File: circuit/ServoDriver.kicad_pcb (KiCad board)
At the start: 2 copper layers, 95 x 54.5 mm, 47 parts, among them IC1 TLP521, IC2 TLP521, IC3 TLP521, IC4 TLP521, IC5 TLP521, IC6 TLP521, J1 RJ45_8pin, J2 RJ45_8pin, J3 servo0, J4 servo1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

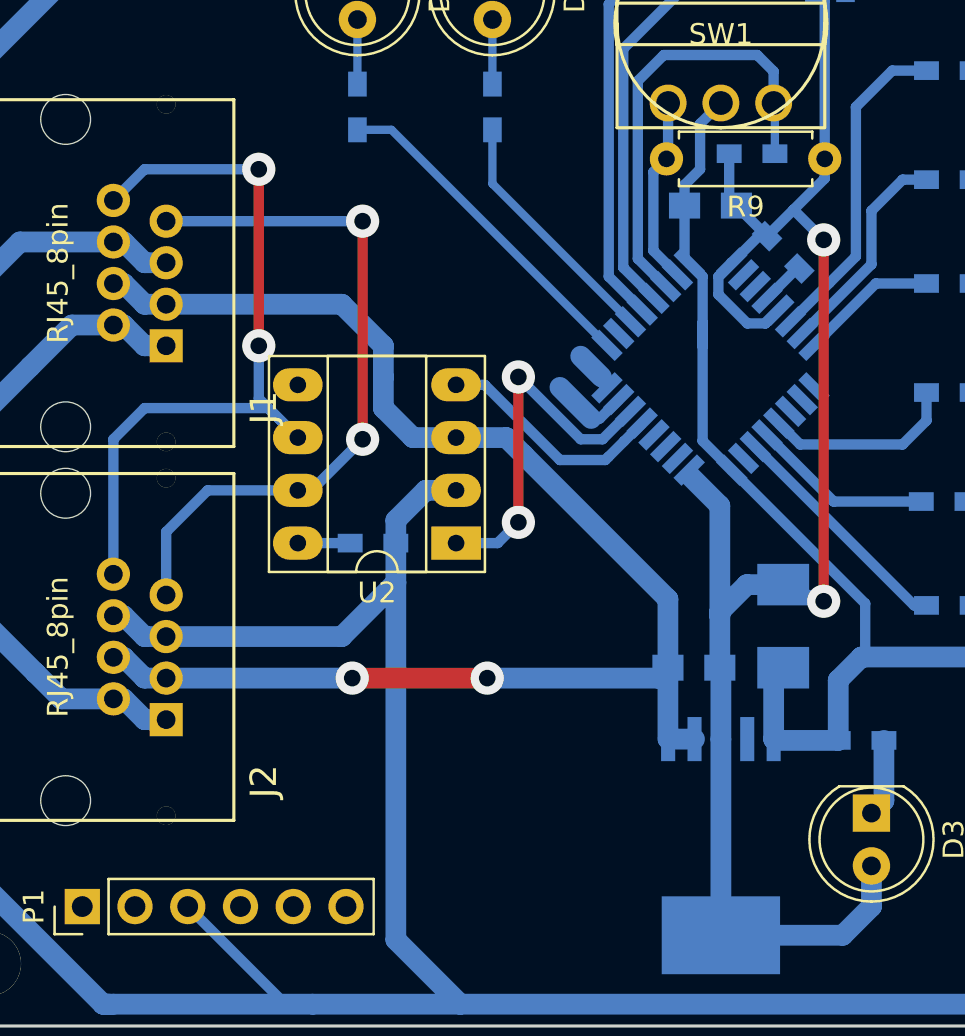
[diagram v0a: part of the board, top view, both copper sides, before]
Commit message: SWDのところにパッドを追加
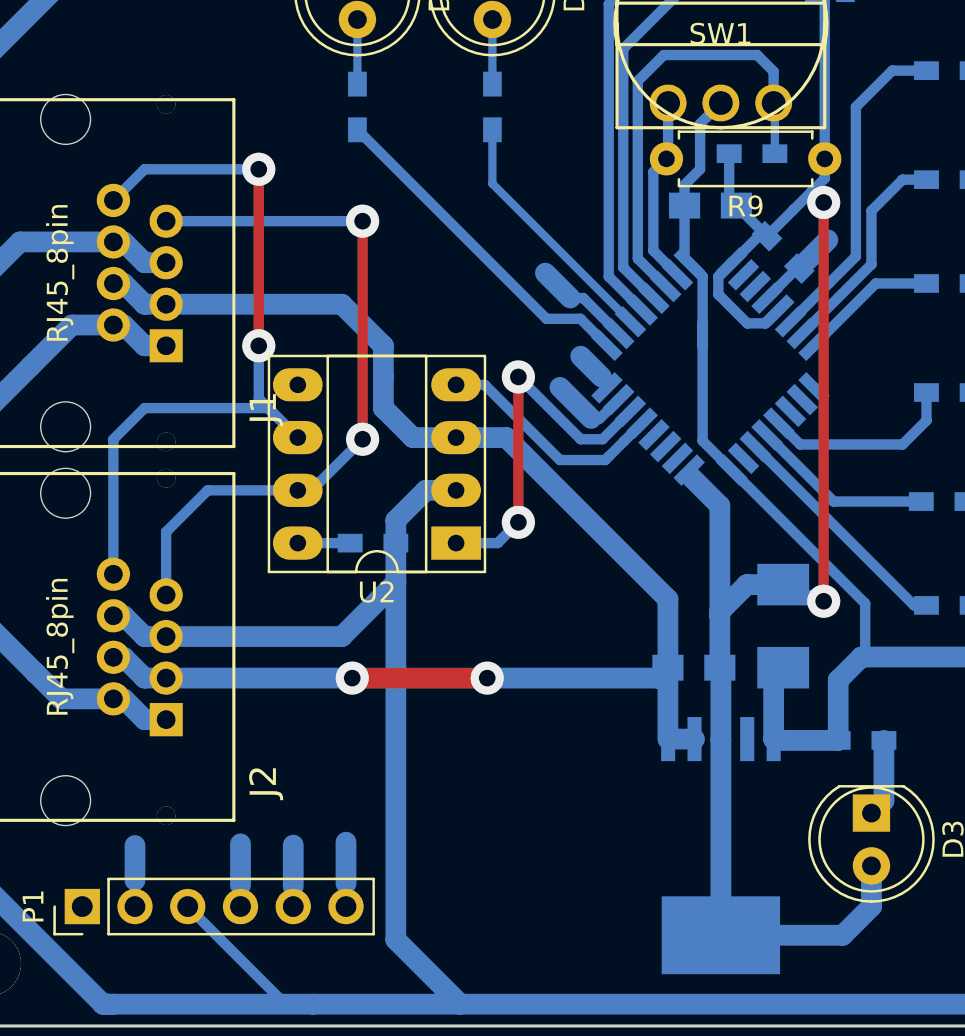
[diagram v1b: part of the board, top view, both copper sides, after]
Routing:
- net /SWO: track 0.00 -> 7.84 mm
- net /NRST: track 2.15 -> 7.06 mm
- net /SWDIO: track 3.83 -> 6.85 mm
- net /SWCLK: track 2.09 -> 5.03 mm
- net +3V3: track 85.5 -> 86.8 mm
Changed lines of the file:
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@@
     (thickness 1.6)
     (drawings 7)
-    (tracks 378)
+    (tracks 395)
     (zones 0)
     (modules 47)
@@
   )
   (setup
-    (last_trace_width 0.5)
+    (last_trace_width 1)
     (user_trace_width 0.4)
     (user_trace_width 1)
@@
   (segment (start 163.5 106) (end 163.5 97.75) (width 1.5) (layer B.Cu) (net 2))
   (segment (start 163.5 97.75) (end 163.5 91) (width 1.5) (layer B.Cu) (net 2))
-  (segment (start 130.747183 94.947183) (end 132.2 96.4) (width 0.5) (layer B.Cu) (net 3))
-  (segment (start 132.2 113.8) (end 130.25 113) (width 0.5) (layer B.Cu) (net 3) (status 800000))
+  (segment (start 132.2 94.6) (end 131.647183 94.047183) (width 0.5) (layer B.Cu) (net 3))
+  (segment (start 130.25 113) (end 132.2 113.8) (width 0.5) (layer B.Cu) (net 3))
   (via (at 132.2 113.8) (size 1.6) (drill 0.8) (layers F.Cu B.Cu) (net 3))
-  (segment (start 132.2 96.4) (end 132.2 113.8) (width 0.5) (layer F.Cu) (net 3))
-  (via (at 132.2 96.4) (size 1.6) (drill 0.8) (layers F.Cu B.Cu) (net 3))
+  (segment (start 132.2 94.6) (end 132.2 113.8) (width 0.5) (layer F.Cu) (net 3))
+  (via (at 132.2 94.6) (size 1.6) (drill 0.8) (layers F.Cu B.Cu) (net 3))
+  (segment (start 132.2 94.6) (end 131.647183 94.047183) (width 0.5) (layer B.Cu) (net 3))
   (segment (start 127.25052 120.4365) (end 127.25052 117.05052) (width 1) (layer B.Cu) (net 3))
   (segment (start 127.25052 117.05052) (end 127.2 117) (width 1) (layer B.Cu) (net 3))
@@
   (segment (start 131.75 84.35) (end 133.25 84.35) (width 0.5) (layer B.Cu) (net 3))
   (segment (start 129.472183 96.222183) (end 130.747183 94.947183) (width 0.5) (layer B.Cu) (net 3))
-  (segment (start 130.747183 94.947183) (end 132.25 93.444366) (width 0.5) (layer B.Cu) (net 3))
+  (segment (start 130.747183 94.947183) (end 131.6 94.094366) (width 0.5) (layer B.Cu) (net 3))
+  (segment (start 131.6 94.094366) (end 132.25 93.444366) (width 0.5) (layer B.Cu) (net 3))
   (segment (start 132.25 93.444366) (end 132.25 92.5) (width 0.5) (layer B.Cu) (net 3))
   (segment (start 132.25 92.5) (end 132.25 84.85) (width 0.5) (layer B.Cu) (net 3))
@@
   (segment (start 129.068019 96.222183) (end 129.472183 96.222183) (width 0.5) (layer B.Cu) (net 3))
   (segment (start 127.775305 97.514897) (end 127.75 97.489592) (width 0.5) (layer B.Cu) (net 3))
-  (segment (start 101.58 128.5) (end 106.28 133.2) (width 0.5) (layer B.Cu) (net 4) (status 400000))
+  (segment (start 101.58 128.5) (end 106.28 133.2) (width 0.5) (layer B.Cu) (net 4))
   (segment (start 106.28 133.2) (end 107.6 133.2) (width 0.5) (layer B.Cu) (net 4))
-  (segment (start 127.775305 107.485103) (end 134.2 113.909798) (width 0.5) (layer B.Cu) (net 4) (status 400000))
+  (segment (start 127.775305 107.485103) (end 134.2 113.909798) (width 0.5) (layer B.Cu) (net 4))
   (segment (start 134.2 113.909798) (end 134.2 116.484) (width 0.5) (layer B.Cu) (net 4))
-  (segment (start 98 96.5) (end 93.5 96.5) (width 1) (layer B.Cu) (net 4) (status 400000))
+  (segment (start 98 96.5) (end 93.5 96.5) (width 1) (layer B.Cu) (net 4))
   (segment (start 93.5 96.5) (end 90.5 99.5) (width 1) (layer B.Cu) (net 4))
-  (segment (start 111.6 111) (end 111.6 109.9) (width 0.5) (layer B.Cu) (net 4) (status 400000))
+  (segment (start 111.6 111) (end 111.6 109.9) (width 0.5) (layer B.Cu) (net 4))
   (segment (start 111.6 112.9) (end 111.6 130.1) (width 1) (layer B.Cu) (net 4))
   (segment (start 111.6 130.1) (end 114.7 133.2) (width 1) (layer B.Cu) (net 4))
@@
   (segment (start 158.5 118.25) (end 158.5 121) (width 1) (layer B.Cu) (net 20))
   (segment (start 156.734 116.484) (end 158.5 118.25) (width 1) (layer B.Cu) (net 20))
-  (segment (start 106.88 108.46) (end 107.54 108.46) (width 0.5) (layer B.Cu) (net 21) (status C00000))
-  (segment (start 107.54 108.46) (end 110 106) (width 0.5) (layer B.Cu) (net 21) (status 400000))
-  (segment (start 110 95.5) (end 100.54 95.5) (width 0.5) (layer B.Cu) (net 21) (status 800000))
+  (segment (start 106.88 108.46) (end 107.54 108.46) (width 0.5) (layer B.Cu) (net 21))
+  (segment (start 107.54 108.46) (end 110 106) (width 0.5) (layer B.Cu) (net 21))
+  (segment (start 110 95.5) (end 100.54 95.5) (width 0.5) (layer B.Cu) (net 21))
   (via (at 110 95.5) (size 1.6) (drill 0.8) (layers F.Cu B.Cu) (net 21))
   (segment (start 110 106) (end 110 95.5) (width 0.5) (layer F.Cu) (net 21))
@@
   (segment (start 98.5 100.5) (end 99.5 101.5) (width 1) (layer B.Cu) (net 22))
   (segment (start 99.5 101.5) (end 100.54 101.5) (width 1) (layer B.Cu) (net 22))
-  (segment (start 106.88 105.92) (end 105 104.04) (width 0.5) (layer B.Cu) (net 23) (status 400000))
-  (segment (start 99.5 93) (end 98 94.5) (width 0.5) (layer B.Cu) (net 23) (status 800000))
+  (segment (start 106.88 105.92) (end 105 104.04) (width 0.5) (layer B.Cu) (net 23))
+  (segment (start 99.5 93) (end 98 94.5) (width 0.5) (layer B.Cu) (net 23))
   (segment (start 105 93) (end 99.5 93) (width 0.5) (layer B.Cu) (net 23))
   (via (at 105 93) (size 1.6) (drill 0.8) (layers F.Cu B.Cu) (net 23))
@@
   (segment (start 99.5 104.5) (end 105.46 104.5) (width 0.5) (layer B.Cu) (net 23))
   (segment (start 98 106) (end 99.5 104.5) (width 0.5) (layer B.Cu) (net 23))
+  (segment (start 99.04 128.5) (end 99.04 127.24) (width 0.5) (layer B.Cu) (net 25) (status 400000))
+  (segment (start 99.04 127.24) (end 99.04 125.56) (width 1) (layer B.Cu) (net 25))
   (segment (start 121.764897 103.525305) (end 121.5 103.260408) (width 0.5) (layer B.Cu) (net 25))
   (segment (start 121.5 103) (end 120.5 102) (width 1) (layer B.Cu) (net 25))
   (segment (start 121.5 103.260408) (end 121.5 103) (width 0.5) (layer B.Cu) (net 25))
   (segment (start 121.764897 103.525305) (end 121.739592 103.5) (width 0.5) (layer B.Cu) (net 25))
+  (segment (start 104.12 128.5) (end 104.12 127.48) (width 0.5) (layer B.Cu) (net 26) (status 400000))
+  (segment (start 104.12 127.48) (end 104.12 125.48) (width 1) (layer B.Cu) (net 26))
   (segment (start 122.330583 104.09099) (end 121.421573 105) (width 0.5) (layer B.Cu) (net 26))
   (segment (start 121 105) (end 119.5 103.5) (width 1) (layer B.Cu) (net 26))
   (segment (start 121.421573 105) (end 121 105) (width 0.5) (layer B.Cu) (net 26))
+  (segment (start 106.66 128.5) (end 106.66 127.54) (width 0.5) (layer B.Cu) (net 27) (status 400000))
+  (segment (start 106.66 127.54) (end 106.66 125.54) (width 1) (layer B.Cu) (net 27))
+  (segment (start 131.027817 97.777817) (end 131.4 97.405634) (width 0.5) (layer B.Cu) (net 27) (status 400000))
+  (segment (start 131.4 97.4) (end 132.4 96.4) (width 1) (layer B.Cu) (net 27))
+  (segment (start 131.4 97.405634) (end 131.4 97.4) (width 0.5) (layer B.Cu) (net 27))
   (segment (start 129.472361 99.211953) (end 130.906497 97.777817) (width 0.5) (layer B.Cu) (net 27))
   (segment (start 130.906497 97.777817) (end 131.027817 97.777817) (width 0.5) (layer B.Cu) (net 27))
+  (segment (start 109.2 128.5) (end 109.2 127.4) (width 0.5) (layer B.Cu) (net 28) (status 400000))
+  (segment (start 109.2 127.4) (end 109.2 125.4) (width 1) (layer B.Cu) (net 28))
+  (segment (start 122.330583 100.90901) (end 120.621573 99.2) (width 0.5) (layer B.Cu) (net 28) (status 400000))
+  (segment (start 120 99.2) (end 118.8 98) (width 1) (layer B.Cu) (net 28))
+  (segment (start 120.621573 99.2) (end 120 99.2) (width 0.5) (layer B.Cu) (net 28))
   (segment (start 116.25 91.1) (end 116.25 93.697056) (width 0.4) (layer B.Cu) (net 29))
   (segment (start 116.25 93.697056) (end 122.896268 100.343324) (width 0.4) (layer B.Cu) (net 29))
-  (segment (start 121.764897 101.474695) (end 111.390202 91.1) (width 0.4) (layer B.Cu) (net 30))
-  (segment (start 111.390202 91.1) (end 109.75 91.1) (width 0.4) (layer B.Cu) (net 30))
+  (segment (start 121.764897 101.474695) (end 120.490202 100.2) (width 0.5) (layer B.Cu) (net 30) (status 400000))
+  (segment (start 118.85 100.2) (end 109.75 91.1) (width 0.5) (layer B.Cu) (net 30) (status 800000))
+  (segment (start 120.490202 100.2) (end 118.85 100.2) (width 0.5) (layer B.Cu) (net 30))
   (segment (start 106.88 111) (end 109.4 111) (width 0.5) (layer B.Cu) (net 31))
   (segment (start 124.71 82.19) (end 126.4 80.5) (width 0.5) (layer B.Cu) (net 32))

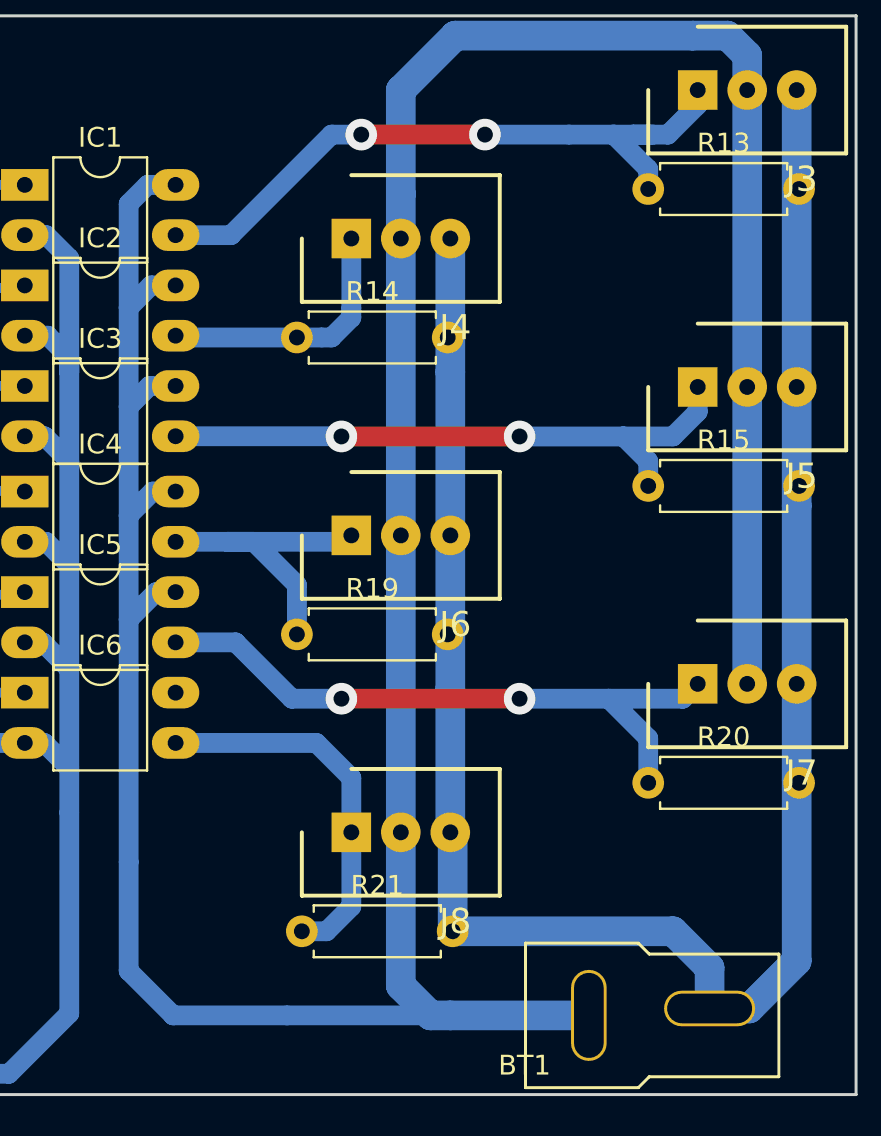
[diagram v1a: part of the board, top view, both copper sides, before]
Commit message: 基板加工用にデータを変更したやつを追加
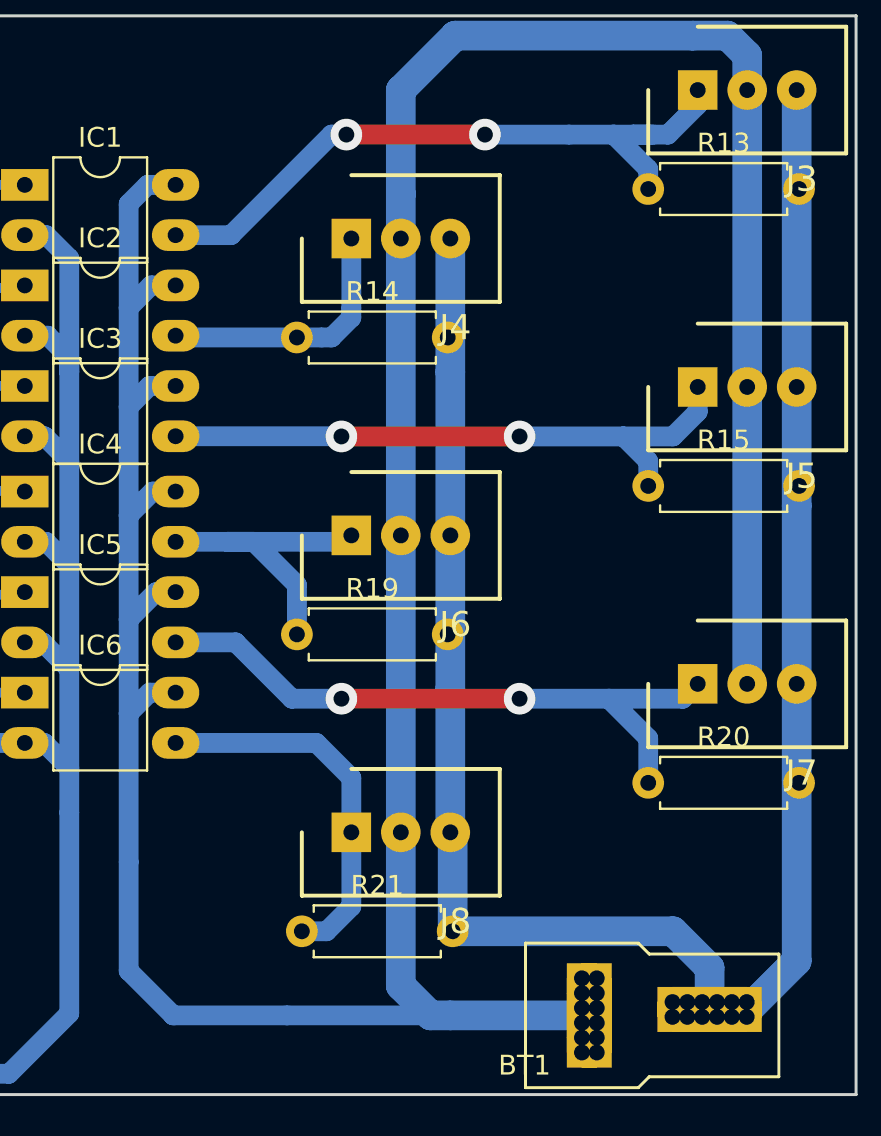
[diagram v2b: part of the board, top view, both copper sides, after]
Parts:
- BT1: footprint YASU:XT_M -> YASU:XT_Mdot
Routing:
- net +7.4V: track 176.3 -> 179.2 mm

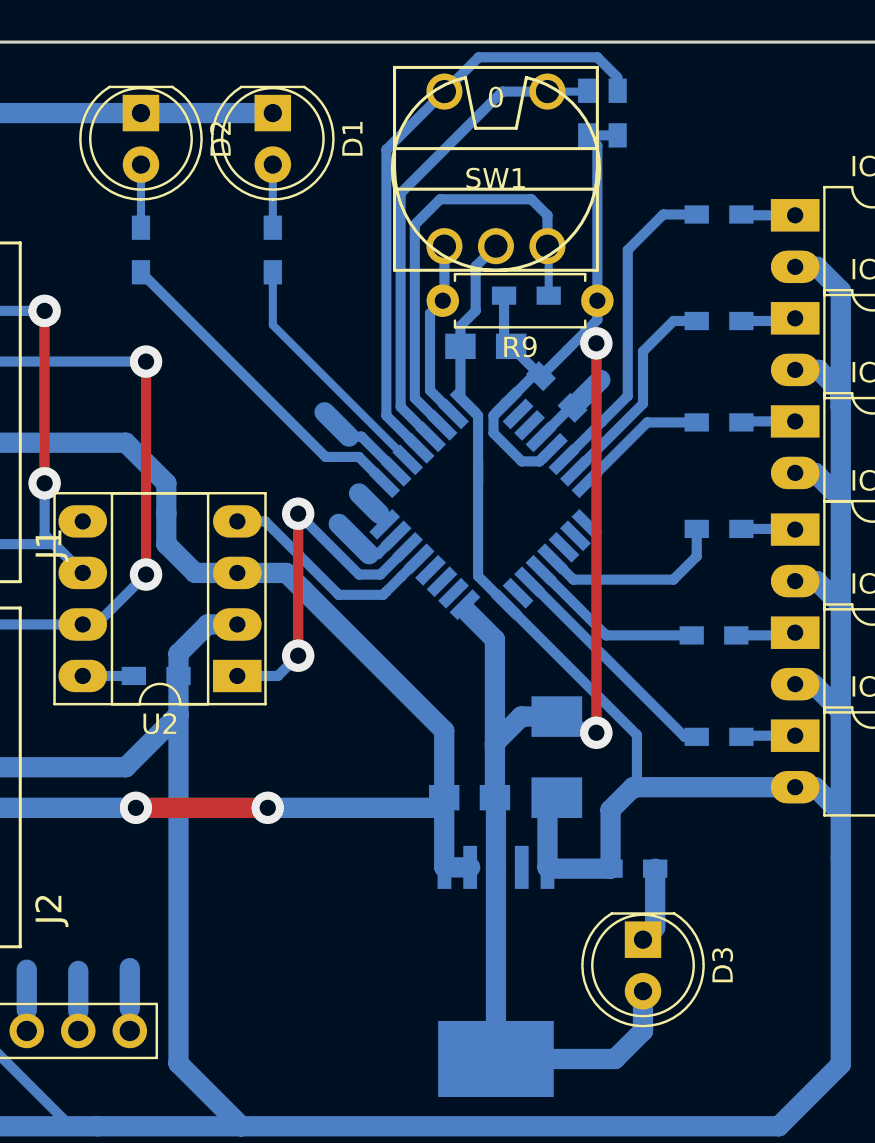
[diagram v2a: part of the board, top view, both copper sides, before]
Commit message: チップ抵抗の大きさ変更とガーバー出力のための手直し
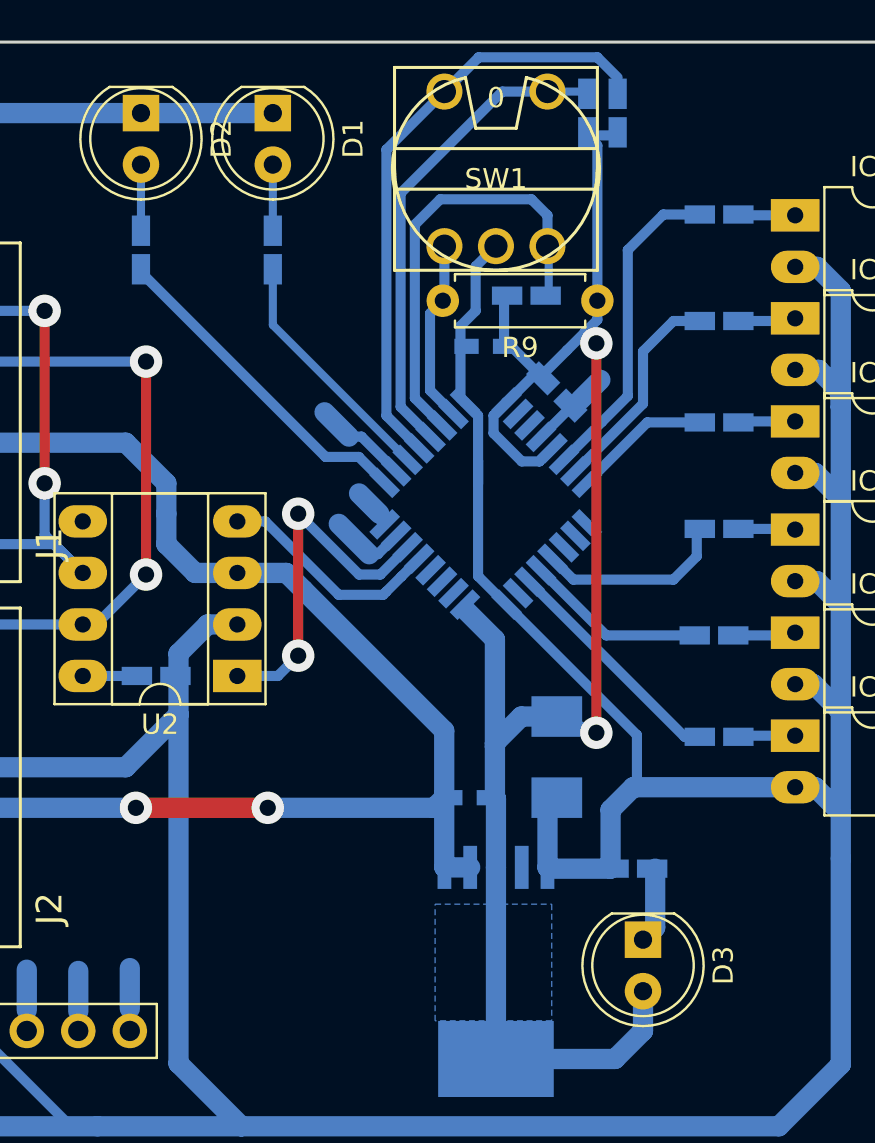
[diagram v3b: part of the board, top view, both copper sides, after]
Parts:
- C1, C2: footprint Capacitors_SMD:C_0805_HandSoldering -> Capacitors_SMD:C_0603_HandSoldering
- R1, R10, R11, R12, R16, R17, R18, R2, R3, R4, R5, R6, R7, R8: footprint Resistors_SMD:R_0603_HandSoldering -> YASU:R_0603_HandSoldering_LP
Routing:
- added copper zone on B.Cu, net +3V3
